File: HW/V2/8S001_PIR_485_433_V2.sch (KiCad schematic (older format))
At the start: 13 parts, among them J1 SWIM, J2 PIR, J3 485, J4 SerIn, J5 RF, SW1 Sw, U1 L78L05_SOT89, U2 STM8S001J3M, U3 SP3485EN

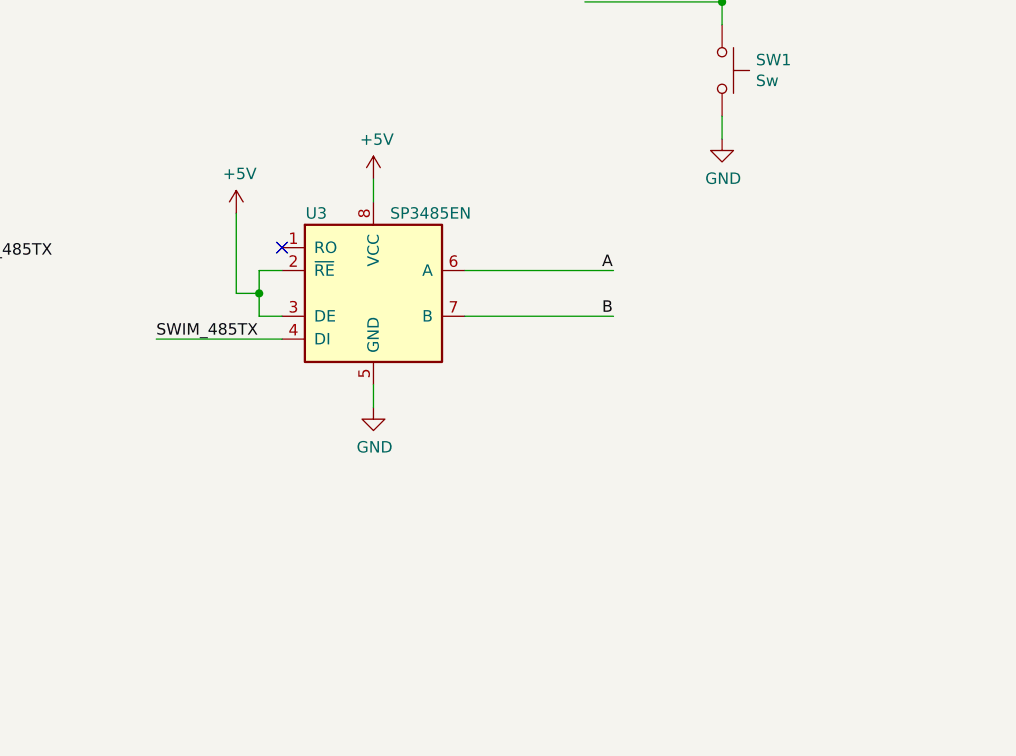
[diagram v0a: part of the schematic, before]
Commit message: V2.1 HW
MAX485 Data Enable wired to BTN signal, now 485 transmitter can be disabled for multimaster mode
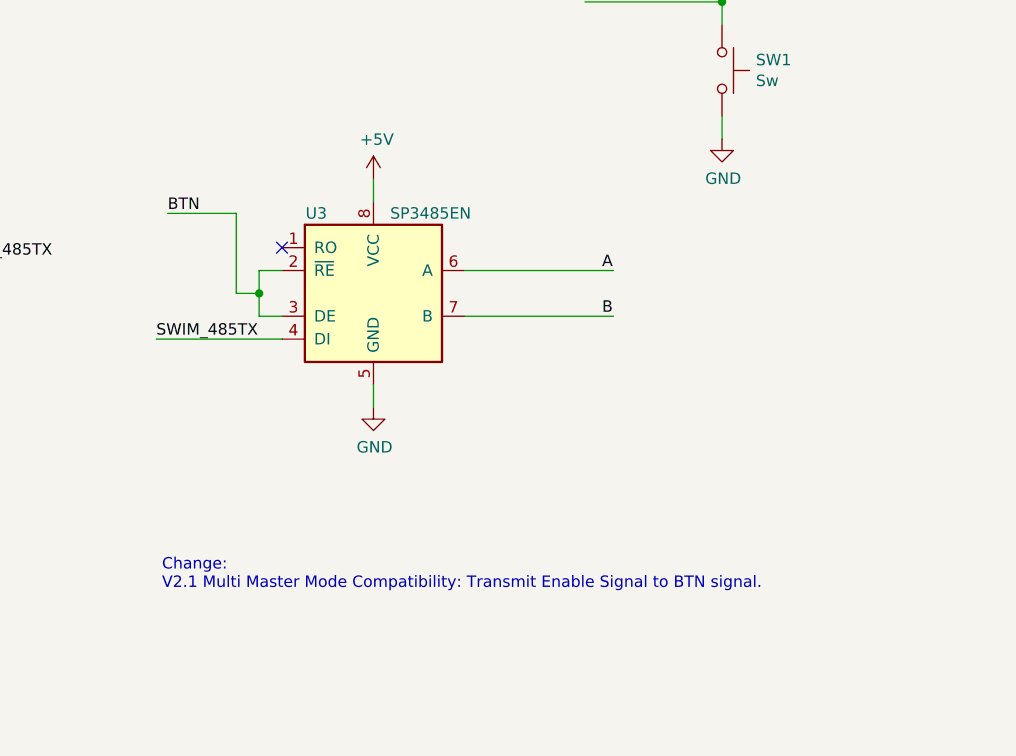
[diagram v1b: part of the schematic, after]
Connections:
- wire segments 65 -> 66
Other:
- note added: "Change:\nV2.1 Multi Master Mode Compatibility: Transmit Enable Signal to BTN signal."
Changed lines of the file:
@@
 Title "PIR Sensor with RS485 Interface"
 Date "2021-01-22"
-Rev "V1.0"
+Rev "V2.1"
 Comp "BK"
 Comment1 ""
@@
 $EndComp
 $Comp
-L power:+5V #PWR011
-U 1 1 601AF92A
-P 5025 2325
-F 0 "#PWR011" H 5025 2175 50  0001 C CNN
-F 1 "+5V" H 5040 2498 50  0000 C CNN
-F 2 "" H 5025 2325 50  0001 C CNN
-F 3 "" H 5025 2325 50  0001 C CNN
-	1    5025 2325
-	1    0    0    -1
-$EndComp
-$Comp
 L power:+5V #PWR010
 U 1 1 601AF9B7
@@
 	1    0    0    -1
 $EndComp
+Wire Wire Line
+	5025 2325 4725 2325
+Text Label 4725 2325 0    50   ~ 0
+BTN
+Text Notes 4700 3975 0    50   ~ 0
+Change:\nV2.1 Multi Master Mode Compatibility: Transmit Enable Signal to BTN signal.
 $EndSCHEMATC
